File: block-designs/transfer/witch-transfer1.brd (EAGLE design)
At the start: 134.6 x 64.4 mm, 18 parts, among them IC1 74LS73N, IC2 74S08N

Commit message: updated files with new images
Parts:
- moved R1 85.3 mm to (125.1, 18.4), turned to 270 degrees
- moved LED1 73.2 mm to (125.1, 29.8), turned to 90 degrees
- moved C4 6.48 mm to (71.1, 41.9)
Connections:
- removed net N$10: IC1.2, JP3.2
- new net N$11: IC1.5, JP2.3
- new net N$12: IC1.9, R1.2
- new net RESET: IC1.2, IC1.6, JP3.2
- net VDD: now also IC1.7
- net VSS: now also IC1.10
- net ZC_TX: no longer R1.2
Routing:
- net RESET: track 0.00 -> 85.7 mm
- net N$11: track 0.00 -> 82.9 mm
- net N$12: track 0.00 -> 81.5 mm
- net N$10: track 69.2 -> 0.00 mm
- net N$8: track 5.08 -> 7.62 mm
- net ZC_TX: track 78.5 -> 80.7 mm
- net N$32: track 169.6 -> 167.8 mm
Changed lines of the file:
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@@
 <?xml version="1.0" encoding="utf-8"?>
 <!DOCTYPE eagle SYSTEM "eagle.dtd">
-<eagle version="6.4">
+<eagle version="6.5.0">
 <drawing>
 <settings>
@@
 <element name="LED2" library="SparkFun-LED" package="LED5MM" value="" x="104.14" y="11.43"/>
 <element name="LED3" library="SparkFun-LED" package="LED5MM" value="" x="104.14" y="46.99"/>
-<element name="LED1" library="SparkFun-LED" package="LED5MM" value="" x="54.61" y="49.53"/>
-<element name="R1" library="resistor" package="0204/5" value="330R" x="45.72" y="49.53" rot="R180"/>
+<element name="LED1" library="SparkFun-LED" package="LED5MM" value="" x="125.095" y="29.845" smashed="yes" rot="R90">
+<attribute name="NAME" x="127" y="34.3916" size="1.27" layer="25" ratio="10" rot="R180"/>
+<attribute name="VALUE" x="126.8984" y="33.0454" size="1.27" layer="27" ratio="10" rot="R90"/>
+</element>
+<element name="R1" library="resistor" package="0204/5" value="330R" x="125.095" y="18.415" rot="R270"/>
 <element name="R2" library="resistor" package="0204/5" value="330R" x="80.01" y="11.43" rot="R180"/>
 <element name="R3" library="resistor" package="0204/5" value="330R" x="78.74" y="46.99" rot="R180"/>
@@
 <element name="C2" library="resistor" package="E2-5" value="" x="5.715" y="27.94"/>
 <element name="C3" library="resistor" package="E2-5" value="" x="120.015" y="48.895"/>
-<element name="C4" library="resistor" package="C025-025X050" value="" x="64.77" y="43.18"/>
+<element name="C4" library="resistor" package="C025-025X050" value="" x="71.12" y="41.91"/>
 <element name="C5" library="resistor" package="C025-025X050" value="" x="93.98" y="36.195" rot="R270"/>
 </elements>
@@
 <contactref element="IC1" pad="1"/>
 <contactref element="JP1" pad="3"/>
-<contactref element="R1" pad="2"/>
-<wire x1="43.18" y1="49.53" x2="43.18" y2="44.45" width="0.254" layer="1"/>
-<wire x1="43.18" y1="44.45" x2="49.53" y2="38.1" width="0.254" layer="1"/>
-<wire x1="49.53" y1="38.1" x2="60.96" y2="38.1" width="0.254" layer="1"/>
 <wire x1="8.89" y1="57.15" x2="8.89" y2="54.61" width="0.254" layer="16"/>
 <wire x1="8.89" y1="54.61" x2="12.7" y2="50.8" width="0.254" layer="16"/>
@@
 <wire x1="26.67" y1="59.69" x2="41.91" y2="59.69" width="0.254" layer="16"/>
 <wire x1="41.91" y1="59.69" x2="43.18" y2="58.42" width="0.254" layer="16"/>
-<wire x1="43.18" y1="58.42" x2="43.18" y2="49.53" width="0.254" layer="16"/>
+<wire x1="43.18" y1="58.42" x2="43.18" y2="40.64" width="0.254" layer="16"/>
+<wire x1="43.18" y1="40.64" x2="45.72" y2="38.1" width="0.254" layer="16"/>
+<wire x1="45.72" y1="38.1" x2="60.96" y2="38.1" width="0.254" layer="16"/>
 </signal>
 <signal name="N$32">
@@
 <wire x1="19.685" y1="52.07" x2="23.495" y2="55.88" width="0.254" layer="16"/>
 <wire x1="23.495" y1="55.88" x2="23.495" y2="59.055" width="0.254" layer="16"/>
-<wire x1="23.495" y1="59.055" x2="25.4" y2="60.96" width="0.254" layer="16"/>
-<wire x1="25.4" y1="60.96" x2="109.22" y2="60.96" width="0.254" layer="16"/>
-<wire x1="109.22" y1="60.96" x2="116.84" y2="53.34" width="0.254" layer="16"/>
-<wire x1="116.84" y1="53.34" x2="121.285" y2="53.34" width="0.254" layer="16"/>
-<wire x1="121.285" y1="53.34" x2="123.19" y2="55.245" width="0.254" layer="16"/>
-<wire x1="123.19" y1="55.245" x2="123.19" y2="57.15" width="0.254" layer="16"/>
+<wire x1="23.495" y1="59.055" x2="26.67" y2="62.23" width="0.254" layer="16"/>
+<wire x1="26.67" y1="62.23" x2="120.65" y2="62.23" width="0.254" layer="16"/>
+<wire x1="120.65" y1="62.23" x2="121.92" y2="60.96" width="0.254" layer="16"/>
+<wire x1="121.92" y1="60.96" x2="121.92" y2="58.42" width="0.254" layer="16"/>
+<wire x1="121.92" y1="58.42" x2="123.19" y2="57.15" width="0.254" layer="16"/>
 </signal>
 <signal name="N$2">
@@
 <contactref element="LED1" pad="A"/>
 <contactref element="R1" pad="1"/>
-<wire x1="48.26" y1="49.53" x2="53.34" y2="49.53" width="0.254" layer="1"/>
+<wire x1="125.095" y1="20.955" x2="125.095" y2="28.575" width="0.254" layer="1"/>
 </signal>
 <signal name="VDD">
@@
 <contactref element="IC1" pad="14"/>
 <contactref element="JP3" pad="1"/>
-<polygon width="0.254" layer="16">
+<polygon width="0.254" layer="16" isolate="0.3048">
 <vertex x="1.27" y="63.5"/>
 <vertex x="133.35" y="63.5"/>
@@
 <contactref element="C1" pad="+"/>
 <contactref element="C4" pad="1"/>
+<contactref element="IC1" pad="7"/>
 </signal>
 <signal name="VSS">
@@
 <contactref element="LED2" pad="K"/>
 <contactref element="LED3" pad="K"/>
-<polygon width="0.254" layer="1">
+<polygon width="0.254" layer="1" isolate="0.3048">
 <vertex x="1.27" y="63.5"/>
 <vertex x="133.35" y="63.5"/>
@@
 <contactref element="C1" pad="-"/>
 <contactref element="C4" pad="2"/>
-</signal>
-<signal name="N$10">
-<contactref element="IC1" pad="2"/>
+<contactref element="IC1" pad="10"/>
+</signal>
+<signal name="RESET">
 <contactref element="JP3" pad="2"/>
 <wire x1="6.35" y1="11.43" x2="6.35" y2="8.89" width="0.254" layer="16"/>
 <wire x1="6.35" y1="8.89" x2="7.62" y2="7.62" width="0.254" layer="16"/>
-<wire x1="7.62" y1="7.62" x2="27.94" y2="7.62" width="0.254" layer="16"/>
-<wire x1="27.94" y1="7.62" x2="55.88" y2="35.56" width="0.254" layer="16"/>
-<wire x1="55.88" y1="35.56" x2="60.96" y2="35.56" width="0.254" layer="16"/>
+<wire x1="7.62" y1="7.62" x2="37.465" y2="7.62" width="0.254" layer="16"/>
+<contactref element="IC1" pad="2"/>
+<contactref element="IC1" pad="6"/>
+<wire x1="37.465" y1="7.62" x2="55.245" y2="25.4" width="0.254" layer="16"/>
+<wire x1="55.245" y1="25.4" x2="60.96" y2="25.4" width="0.254" layer="16"/>
+<wire x1="60.96" y1="25.4" x2="56.515" y2="25.4" width="0.254" layer="1"/>
+<wire x1="56.515" y1="25.4" x2="54.61" y2="27.305" width="0.254" layer="1"/>
+<wire x1="54.61" y1="27.305" x2="54.61" y2="33.655" width="0.254" layer="1"/>
+<wire x1="54.61" y1="33.655" x2="56.515" y2="35.56" width="0.254" layer="1"/>
+<wire x1="56.515" y1="35.56" x2="60.96" y2="35.56" width="0.254" layer="1"/>
+</signal>
+<signal name="N$11">
+<contactref element="JP2" pad="3"/>
+<contactref element="IC1" pad="5"/>
+<wire x1="120.65" y1="57.15" x2="120.65" y2="53.975" width="0.254" layer="16"/>
+<wire x1="120.65" y1="53.975" x2="119.38" y2="52.705" width="0.254" layer="16"/>
+<wire x1="119.38" y1="52.705" x2="72.39" y2="52.705" width="0.254" layer="16"/>
+<wire x1="72.39" y1="52.705" x2="64.77" y2="45.085" width="0.254" layer="16"/>
+<wire x1="64.77" y1="45.085" x2="64.77" y2="29.21" width="0.254" layer="16"/>
+<wire x1="64.77" y1="29.21" x2="63.5" y2="27.94" width="0.254" layer="16"/>
+<wire x1="63.5" y1="27.94" x2="60.96" y2="27.94" width="0.254" layer="16"/>
+</signal>
+<signal name="N$12">
+<contactref element="IC1" pad="9"/>
+<contactref element="R1" pad="2"/>
+<wire x1="68.58" y1="25.4" x2="71.12" y2="25.4" width="0.254" layer="16"/>
+<wire x1="71.12" y1="25.4" x2="73.025" y2="23.495" width="0.254" layer="16"/>
+<wire x1="73.025" y1="23.495" x2="73.025" y2="8.255" width="0.254" layer="16"/>
+<wire x1="73.025" y1="8.255" x2="75.565" y2="5.715" width="0.254" layer="16"/>
+<wire x1="75.565" y1="5.715" x2="121.285" y2="5.715" width="0.254" layer="16"/>
+<wire x1="121.285" y1="5.715" x2="125.095" y2="9.525" width="0.254" layer="16"/>
+<wire x1="125.095" y1="9.525" x2="125.095" y2="15.875" width="0.254" layer="16"/>
 </signal>
 </signals>

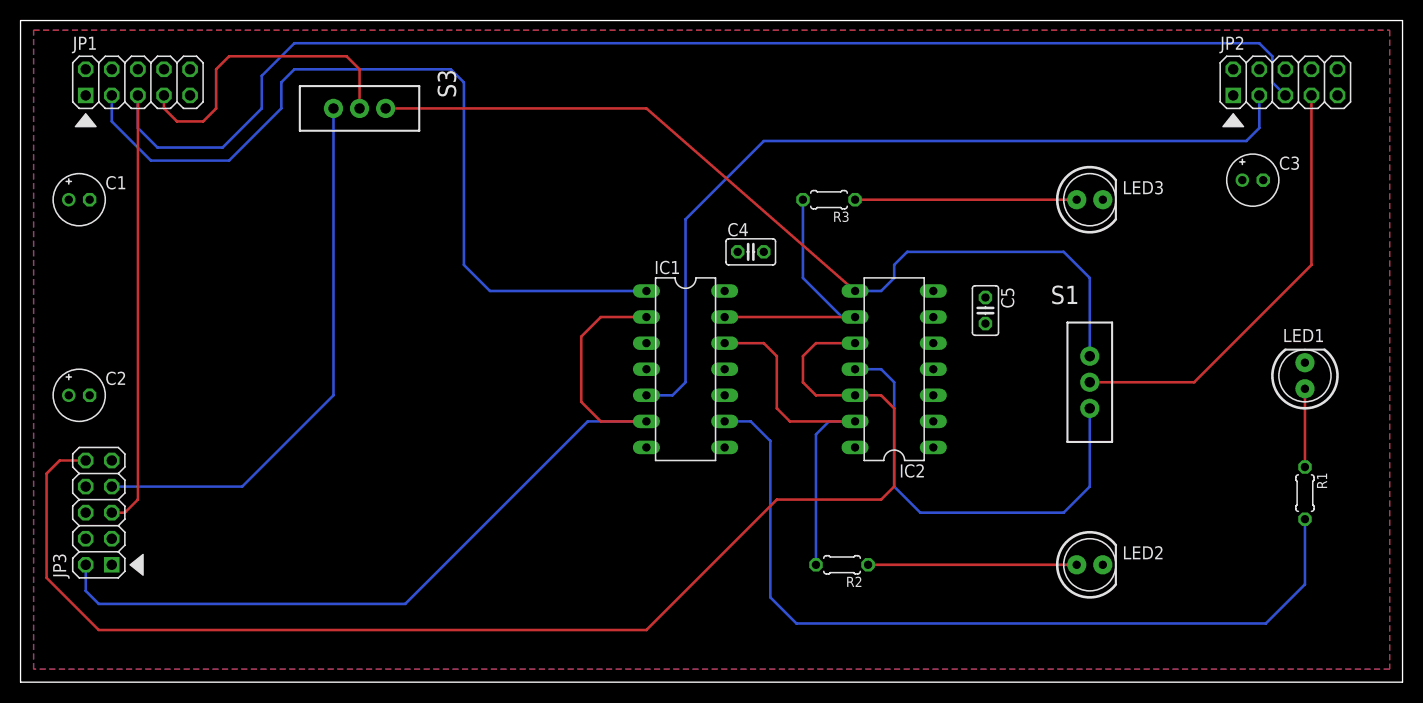
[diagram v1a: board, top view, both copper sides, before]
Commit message: updated pdf schematics and board files with fixes
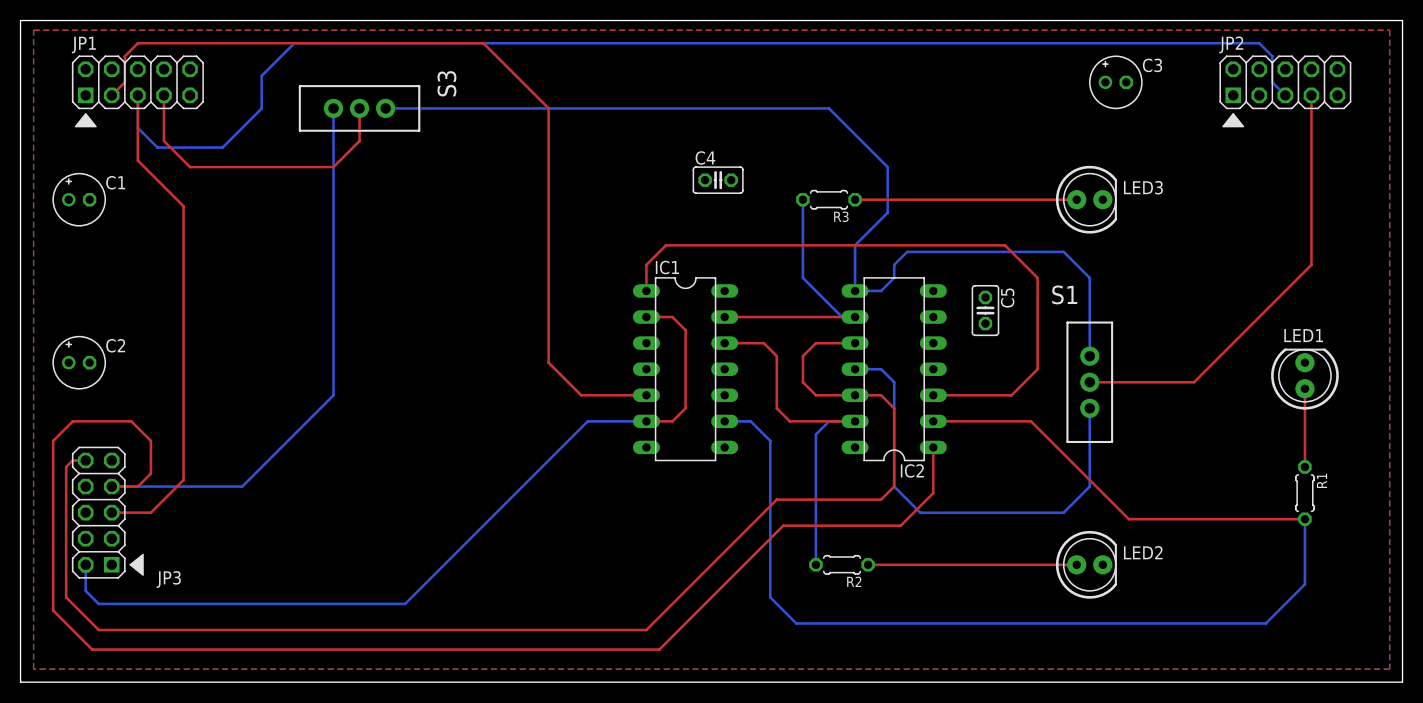
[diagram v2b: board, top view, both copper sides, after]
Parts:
- moved C3 16.4 mm to (106.7, 58.4)
- moved C4 7.67 mm to (67.9, 48.9)
- moved C2 3.17 mm to (5.71, 31.1)
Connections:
- removed net N$12: IC1.9, R1.2
- removed net N$9: JP3.7, S3.3
- removed net ZC_TX: IC1.1, JP1.3
- new net 10A_PULSES: IC2.1, JP3.7, S3.3
- new net ZC: IC1.5, JP1.3
- new net ZC_OUTPUT: IC1.9, IC2.2, R1.2
- net N$11: now also IC1.1, IC2.3; no longer IC1.5, JP2.3
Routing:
- net 10A_PULSES: track 0.00 -> 186.4 mm
- net ZC_OUTPUT: track 0.00 -> 121.7 mm
- net ZC: track 0.00 -> 84.4 mm
- net N$12: track 81.5 -> 0.00 mm
- net ZC_TX: track 80.7 -> 0.00 mm
- net N$9: track 53.2 -> 0.00 mm
- net N$11: track 82.9 -> 62.8 mm
- net N$43: track 86.3 -> 98.5 mm
- net N$32: track 167.8 -> 173.0 mm
- net RESET: track 85.7 -> 81.3 mm
- net N$2: track 130.6 -> 128.3 mm
- net TRANSFER_PULSE: track 30.0 -> 28.8 mm
